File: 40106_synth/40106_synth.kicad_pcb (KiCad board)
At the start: 2 copper layers, 99 x 99 mm, 56 parts, among them J1 Conn_01x01, J100 Conn_01x06, J101 Conn_01x02, J11 Conn_01x01, J12 Conn_01x01, J13 Conn_01x02, J14 Conn_01x02, J16 Conn_02x03_Counter_Clockwise, J18 Conn_01x02, J19 Conn_01x01, J2 Conn_01x02, J21 Conn_01x02, J22 Conn_01x02, J23 Conn_01x01, J24 Conn_01x01, J25 Conn_01x01, J26 Conn_01x01, J27 Conn_01x02, J28 Conn_01x02, J29 Conn_01x02, J3 Conn_01x02, J30 Conn_01x01, J31 Conn_01x01, J32 Audio-Jack-3, J4 Conn_01x01, J5 Conn_01x02, J7 Conn_01x01, J8 Conn_01x01, J9 Conn_01x02, SW1 SW_DIP_x02, U1 40106

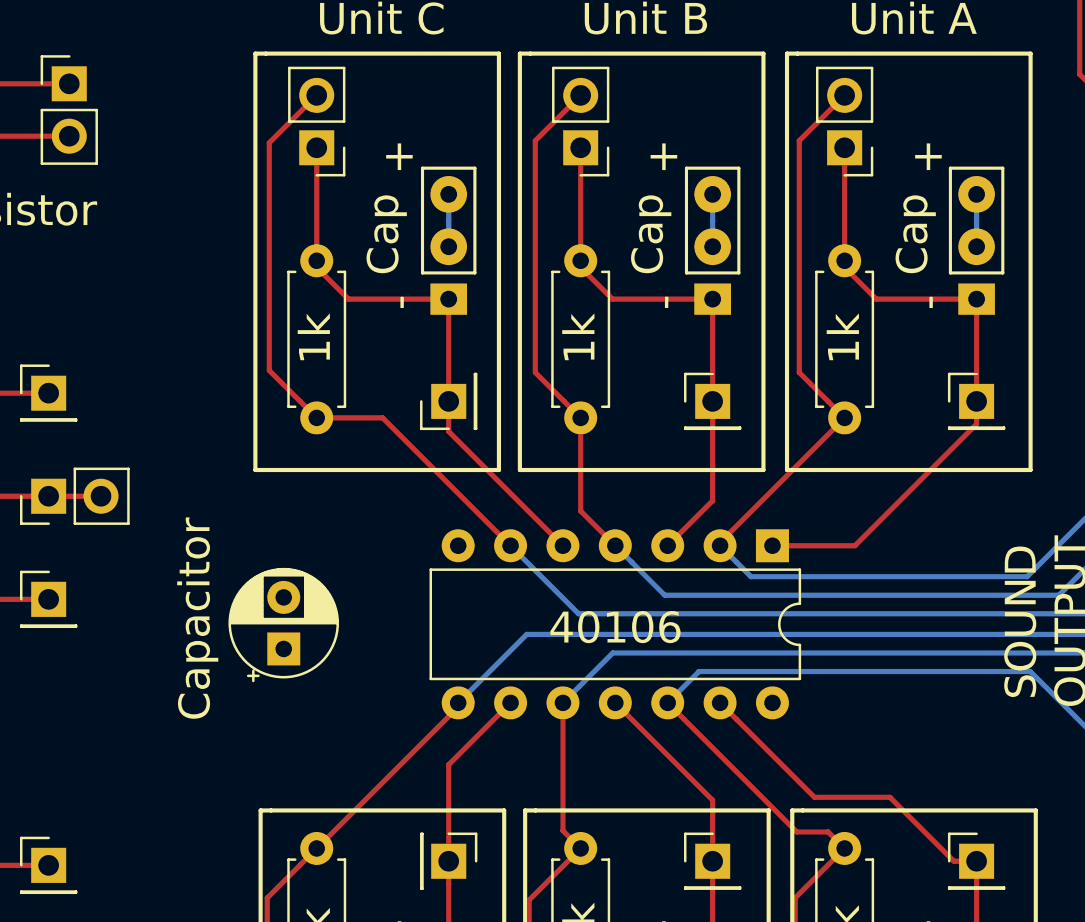
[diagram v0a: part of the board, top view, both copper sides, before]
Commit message: Add licence. Add README. Add model setups. Touch up silkscreen.
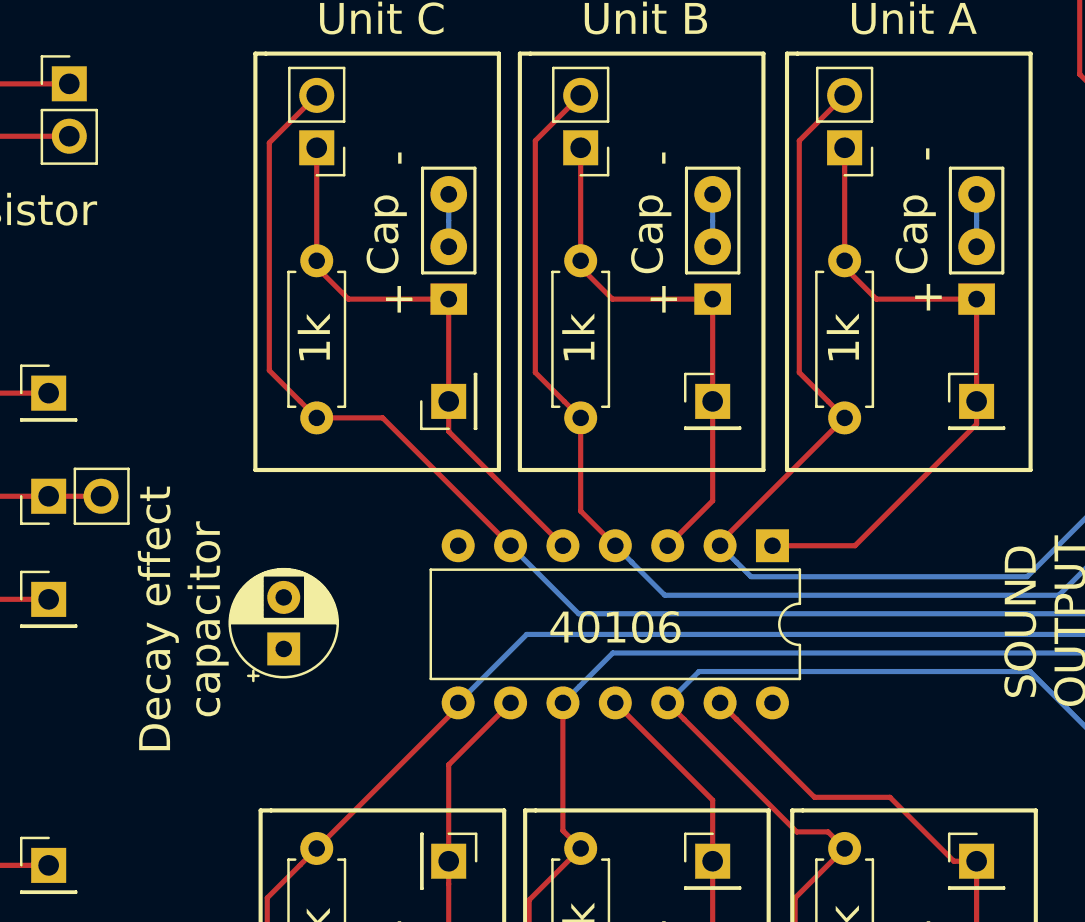
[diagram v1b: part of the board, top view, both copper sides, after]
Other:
- board text added: "Decay effect capacitor"
- board text added: "TAPR Licence"
- board text removed: "Capacitor"
- board text removed: "Designed by Jakub Zalesak for Engineers Without Borders"
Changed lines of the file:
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@@
   (page A4)
   (layers
-    (0 F.Cu signal)
-    (31 B.Cu signal)
+    (0 F.Cu signal hide)
+    (31 B.Cu signal hide)
     (32 B.Adhes user hide)
     (33 F.Adhes user hide)
@@
     )
   )
+  (gr_text "TAPR Licence" (at 77.9 95.6) (layer B.SilkS)
+    (effects (font (size 1.5 1.5) (thickness 0.3)))
+  )
   (gr_text "Notes:\n- Board is designed for atypical jack connector, a different footprint is recommended\n- Duplicating pins on divider is recommended\n- All unlabeled are pins\n- Board is designed for small resistors, use lager pin separation for standard size" (at 45.085 187.325) (layer Cmts.User)
     (effects (font (size 1.5 1.5) (thickness 0.3)) (justify left))
@@
     (effects (font (size 1.5 1.5) (thickness 0.3)))
   )
-  (gr_text - (at 105.664 131.699 90) (layer F.SilkS)
-    (effects (font (size 1.5 1.5) (thickness 0.3)))
-  )
-  (gr_text + (at 80.01 124.587) (layer F.SilkS)
-    (effects (font (size 1.5 1.5) (thickness 0.3)))
-  )
-  (gr_text - (at 80.01 131.699 90) (layer F.SilkS)
-    (effects (font (size 1.5 1.5) (thickness 0.3)))
-  )
-  (gr_text - (at 92.837 131.699 90) (layer F.SilkS)
+  (gr_text - (at 105.5 124.5 90) (layer F.SilkS)
+    (effects (font (size 1.5 1.5) (thickness 0.3)))
+  )
+  (gr_text + (at 80 131.5) (layer F.SilkS)
+    (effects (font (size 1.5 1.5) (thickness 0.3)))
+  )
+  (gr_text - (at 79.9 124.7 90) (layer F.SilkS)
+    (effects (font (size 1.5 1.5) (thickness 0.3)))
+  )
+  (gr_text - (at 92.7 124.7 90) (layer F.SilkS)
     (effects (font (size 1.5 1.5) (thickness 0.3)))
   )
@@
     (effects (font (size 1.5 1.5) (thickness 0.3)))
   )
-  (gr_text + (at 105.664 124.587) (layer F.SilkS)
-    (effects (font (size 1.5 1.5) (thickness 0.3)))
-  )
-  (gr_text + (at 92.837 124.587) (layer F.SilkS)
+  (gr_text + (at 105.664 131.4) (layer F.SilkS)
+    (effects (font (size 1.5 1.5) (thickness 0.3)))
+  )
+  (gr_text + (at 92.837 131.5) (layer F.SilkS)
     (effects (font (size 1.5 1.5) (thickness 0.3)))
   )
@@
     (effects (font (size 1.5 1.5) (thickness 0.3)))
   )
-  (gr_text Capacitor (at 70.104 147.066 90) (layer F.SilkS)
+  (gr_text "Decay effect \ncapacitor" (at 69.4 147.1 90) (layer F.SilkS)
     (effects (font (size 1.5 1.5) (thickness 0.3)))
   )
@@
     (effects (font (size 1.5 1.5) (thickness 0.3)))
   )
-  (gr_text "Designed by Jakub Zalesak\nfor Engineers Without Borders" (at 77.609204 100.2) (layer B.SilkS)
-    (effects (font (size 1.5 1.5) (thickness 0.3)))
-  )
